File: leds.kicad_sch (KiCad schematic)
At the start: 10 parts, among them U10 SK9822, U11 SK9822, U12 SK9822, U13 SK9822, U14 SK9822

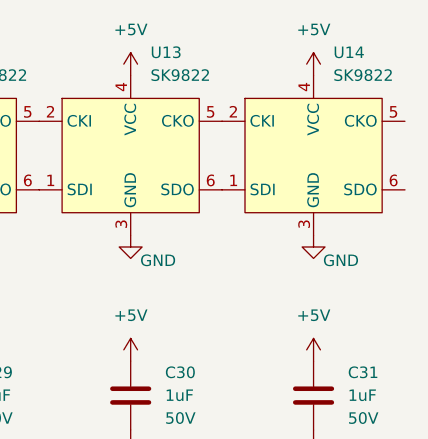
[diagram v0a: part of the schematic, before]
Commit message: Fixed most DRC errors, but need to relayout RFO/RFI
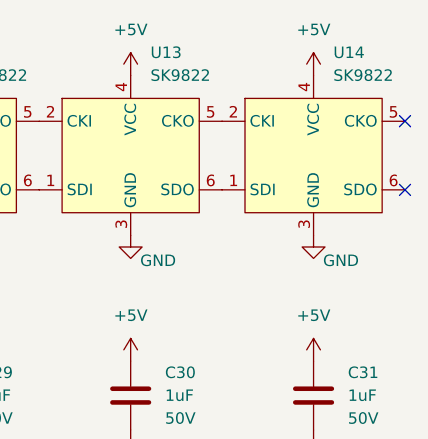
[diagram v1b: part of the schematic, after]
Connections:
- no-connect marks 0 -> 2
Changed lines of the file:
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@@
 	(generator_version "8.0")
 	(paper "A4")
+	(no_connect
+		(at 201.93 90.17)
+	)
+	(no_connect
+		(at 201.93 82.55)
+	)
 	(wire
 		(pts

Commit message: Optimizing components for ordering
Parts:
- C27, C28, C29, C30, C31: LCSC Part # (none) -> C28323
- U10, U11, U12, U13, U14: LCSC Part # (none) -> C5378730
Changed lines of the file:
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@@
+			)
+		)
+		(property "LCSC Part #" "C5378730"
+			(at 110.49 80.01 0)
+			(effects
+				(font
+					(size 1.27 1.27)
+				)
+				(hide yes)
 			)
 		)
@@
 			)
 		)
+		(property "LCSC Part #" "C5378730"
+			(at 171.45 80.01 0)
+			(effects
+				(font
+					(size 1.27 1.27)
+				)
+				(hide yes)
+			)
+		)
 		(pin "4"
 		)
@@
 			)
 		)
+		(property "LCSC Part #" "C28323"
+			(at 151.13 113.03 0)
+			(effects
+				(font
+					(size 1.27 1.27)
+				)
+				(hide yes)
+			)
+		)
 		(pin "1"
 		)
@@
 			)
 		)
+		(property "LCSC Part #" "C5378730"
+			(at 151.13 80.01 0)
+			(effects
+				(font
+					(size 1.27 1.27)
+				)
+				(hide yes)
+			)
+		)
 		(pin "4"
 		)
@@
 			)
 		)
+		(property "LCSC Part #" "C5378730"
+			(at 191.77 80.01 0)
+			(effects
+				(font
+					(size 1.27 1.27)
+				)
+				(hide yes)
+			)
+		)
 		(pin "4"
 		)
@@
 			)
 		)
+		(property "LCSC Part #" "C5378730"
+			(at 130.81 80.01 0)
+			(effects
+				(font
+					(size 1.27 1.27)
+				)
+				(hide yes)
+			)
+		)
 		(pin "4"
 		)
@@
 			)
 		)
+		(property "LCSC Part #" "C28323"
+			(at 110.49 113.03 0)
+			(effects
+				(font
+					(size 1.27 1.27)
+				)
+				(hide yes)
+			)
+		)
 		(pin "1"
 		)
@@
 			)
 		)
+		(property "LCSC Part #" "C28323"
+			(at 191.77 113.03 0)
+			(effects
+				(font
+					(size 1.27 1.27)
+				)
+				(hide yes)
+			)
+		)
 		(pin "1"
 		)
@@
 			)
 		)
+		(property "LCSC Part #" "C28323"
+			(at 130.81 113.03 0)
+			(effects
+				(font
+					(size 1.27 1.27)
+				)
+				(hide yes)
+			)
+		)
 		(pin "1"
 		)
@@
 			(at 171.45 113.03 0)
 			(effects
+				(font
+					(size 1.27 1.27)
+				)
+				(hide yes)
+			)
+		)
+		(property "LCSC Part #" "C28323"
+			(at 171.45 113.03 0)
+			(effects
